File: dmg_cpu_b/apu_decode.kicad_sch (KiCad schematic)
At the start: 67 parts

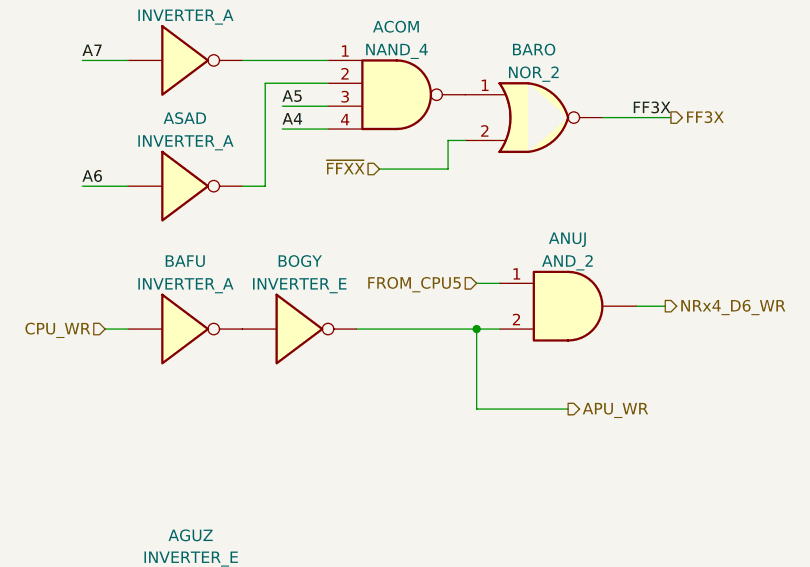
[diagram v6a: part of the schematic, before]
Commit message: VRAM interface sheet added but various edits in existing sheets. Notable merge of RESET, CLOCKS and FF04 DIV sheets
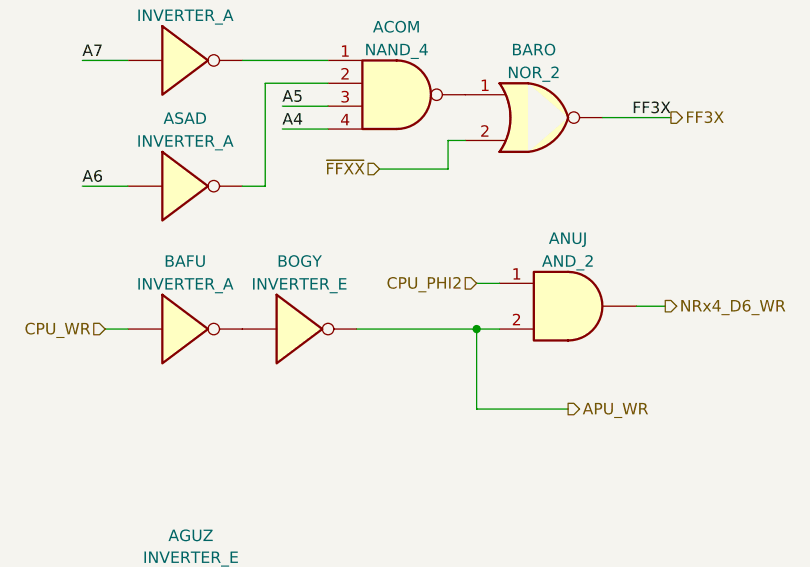
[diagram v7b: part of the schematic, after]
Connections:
- net FROM_CPU5 renamed CPU_PHI2
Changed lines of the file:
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@@
   (title_block
     (title "DMG CPU B")
-    (date "2022-03-12")
+    (date "2022-05-02")
     (rev "0")
     (company "CC-BY-SA-4.0 Régis Galland & Michael Singer -- Derived work from Furrtek")
@@
     (effects (font (size 1.27 1.27)) (justify right))
   )
-  (hierarchical_label "FROM_CPU5" (shape input) (at 97.79 175.895 180)
+  (hierarchical_label "CPU_PHI2" (shape input) (at 97.79 175.895 180)
     (effects (font (size 1.27 1.27)) (justify right))
   )
